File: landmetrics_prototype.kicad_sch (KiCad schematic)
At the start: 6 parts, among them U1 MMA8653FCR1, U2 MMA8653FCR1, U3 MMA8653FCR1

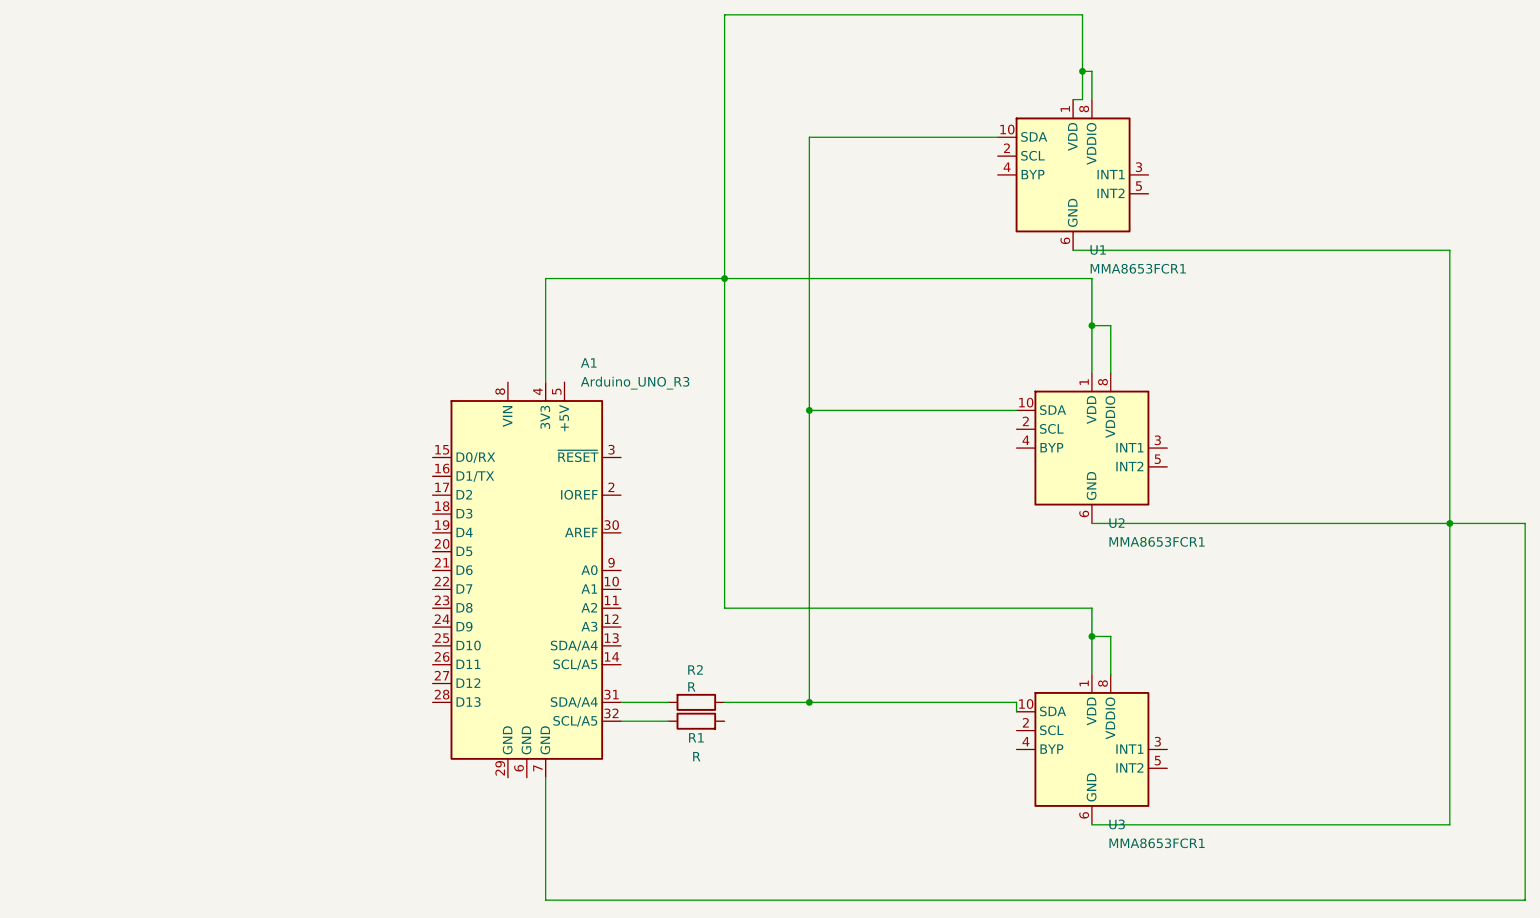
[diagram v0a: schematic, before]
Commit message: Adding LEDs... Still need to add Button with debouncing capacitor!
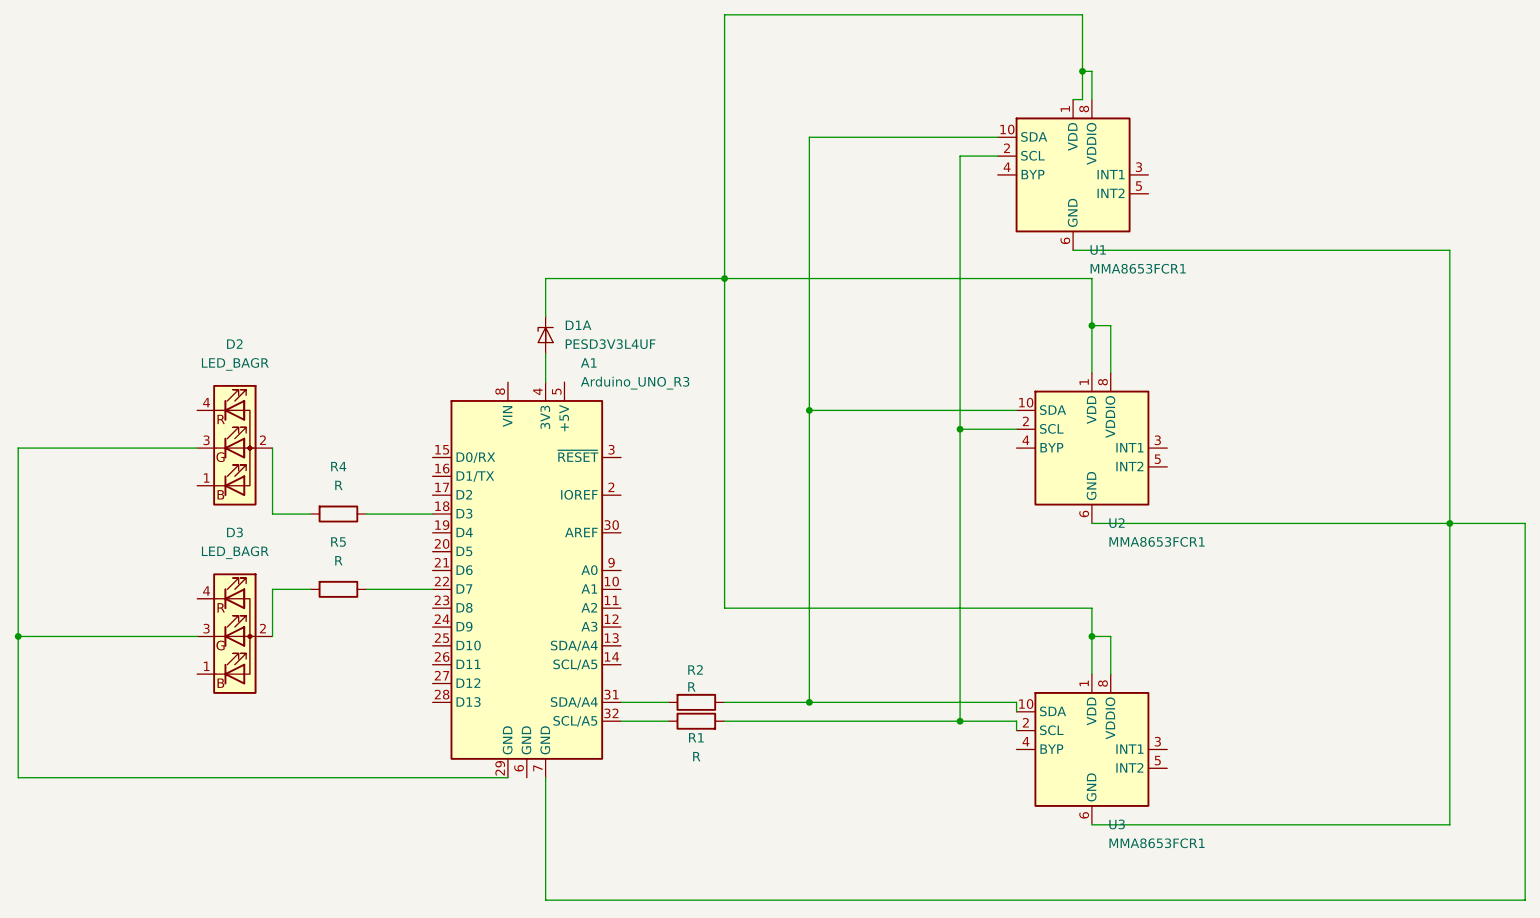
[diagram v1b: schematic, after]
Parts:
- added D1: PESD3V3L4UF, Package_TO_SOT_SMD:SOT-886, symbol Power_Protection:PESD3V3L4UF
- added D2, D3: LED_BAGR, symbol Device:LED_BAGR
- added R4, R5: R, symbol Device:R
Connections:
- net at R1.2: now also U1.2 (SCL), U2.2 (SCL), U3.2 (SCL)
- net at U1.1 (VDD), U1.8 (VDDIO), U2.1 (VDD)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: now also D1.1 (K1); no longer A1.4 (3V3)
- net at A1.18 (D3): now also R4.1
- net at A1.22 (D7): now also R5.1
- net at A1.29 (GND): now also D2.3 (GK), D3.3 (GK)
- new net: D3.2 (A), R5.2
- new net: D2.2 (A), R4.2
- new net: A1.4 (3V3), D1.2 (A), D1.5 (A)

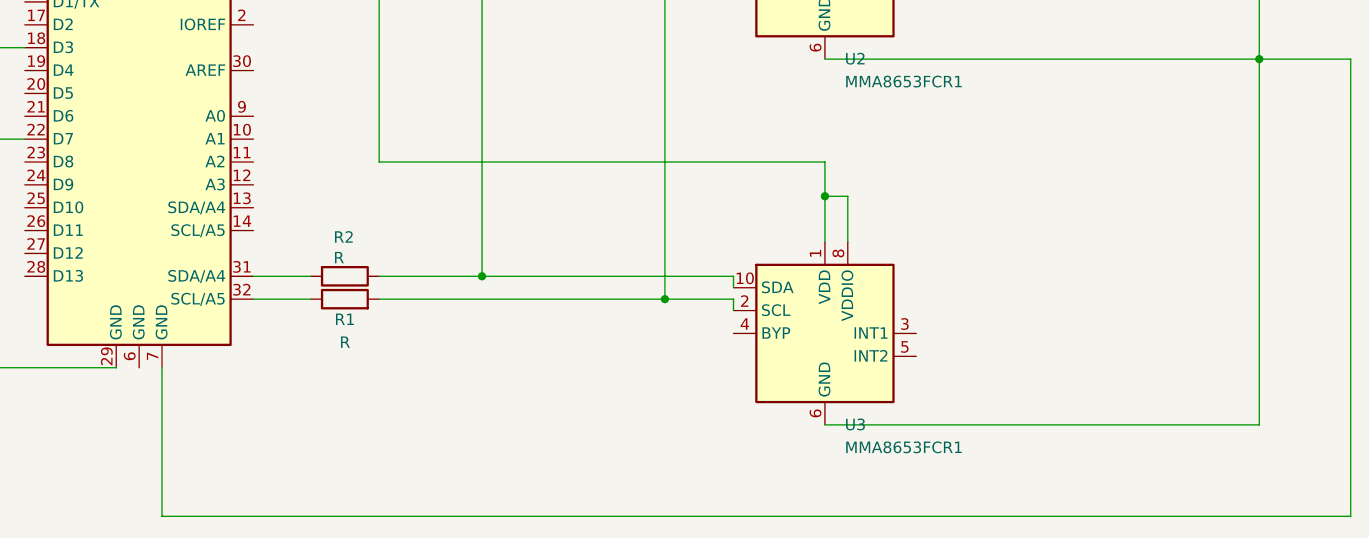
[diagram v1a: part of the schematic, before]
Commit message: Starting edits based on Dr. Cameron's comments/critiques... Adding a makeshift to-do document to be transfered to our GDrive
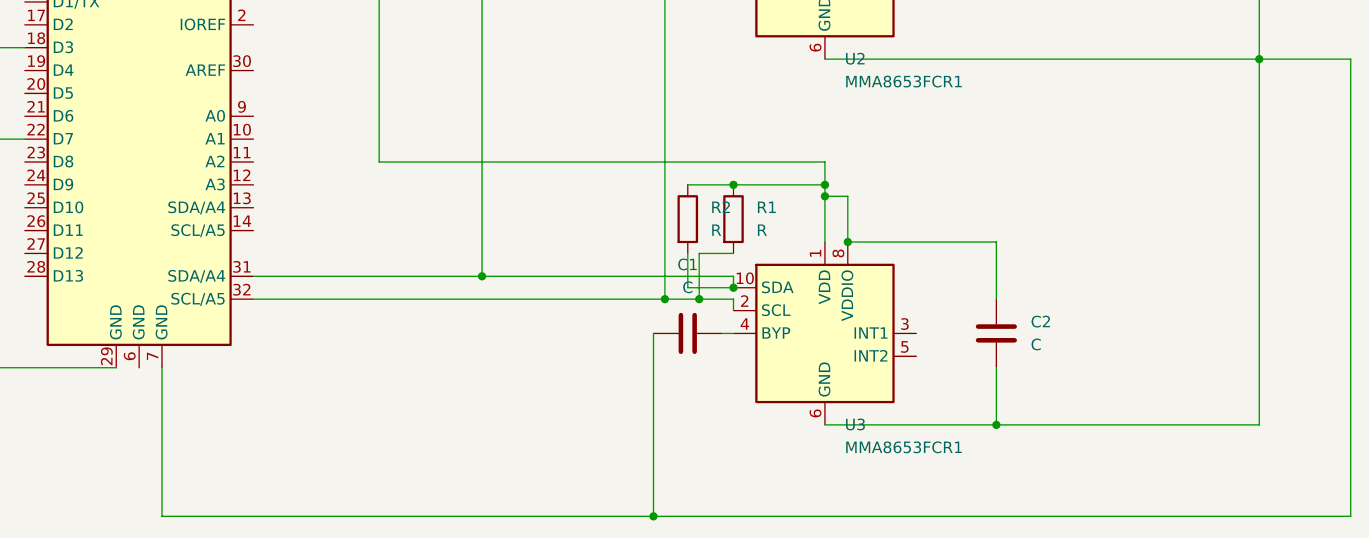
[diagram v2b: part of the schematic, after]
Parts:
- added C1, C2: C, symbol Device:C
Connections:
- net at R1.1: now also D1.1 (K1), R2.1, U1.1 (VDD), U1.8 (VDDIO), U2.1 (VDD), U2.8 (VDDIO), U3.1 (VDD), U3.8 (VDDIO), C2.1; no longer A1.32 (SCL/A5)
- net at R1.2, U1.2 (SCL), U2.2 (SCL)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: now also A1.32 (SCL/A5)
- net at U1.10 (SDA), U2.10 (SDA), U3.10 (SDA): now also A1.31 (SDA/A4), R2.2; no longer R2.1
- net at U3.4 (BYP): now also C1.1
- net at A1.7 (GND), U1.6 (GND), U1.7 (GND)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: now also C1.2, C2.2
